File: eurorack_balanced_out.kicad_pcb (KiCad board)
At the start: 2 copper layers, 60 x 35 mm, 31 parts, among them J1 Conn_01x02, J2 Conn_01x02, J3 Conn_02x05_Odd_Even, J4 AudioJack3, J5 AudioJack3, U1 THAT1646W16, U2 THAT1646W16

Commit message: fix silkscreen
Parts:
- removed J2: Conn_01x02, Connector_PinHeader_2.54mm:PinHeader_1x02_P2.54mm_Vertical
- added Right in: Conn_01x02, Connector_PinHeader_2.54mm:PinHeader_1x02_P2.54mm_Vertical, F.Cu at (155.0, 144.5)
- Left in: renamed from J1
- Left out: renamed from J5
- Power in: renamed from J3
- Right out: renamed from J4
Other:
- board text added: "Patchnut eurorack balanced output https://github.com/mendelt/eurorack_balanced_out"
- board text added: "balanced stereo outs"
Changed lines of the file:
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@@
   (general
     (thickness 1.6)
-    (drawings 4)
+    (drawings 7)
     (tracks 155)
     (zones 0)
@@
     (tags "capacitor electrolytic")
     (attr smd)
-    (fp_text reference C1 (at 0 4) (layer F.SilkS)
+    (fp_text reference C1 (at 2 2.5) (layer F.SilkS)
       (effects (font (size 1 1) (thickness 0.15)))
     )
@@
     (tags "capacitor electrolytic")
     (attr smd)
-    (fp_text reference C2 (at 0 -4.35) (layer F.SilkS)
+    (fp_text reference C2 (at -1.5 -2.5) (layer F.SilkS)
       (effects (font (size 1 1) (thickness 0.15)))
     )
@@
     (tags "capacitor handsolder")
     (attr smd)
-    (fp_text reference C3 (at -2.975 0) (layer F.SilkS)
+    (fp_text reference C3 (at 3 0) (layer F.SilkS)
       (effects (font (size 1 1) (thickness 0.15)))
     )
@@
     (tags "capacitor electrolytic")
     (attr smd)
-    (fp_text reference C5 (at 0 -3.7 90) (layer F.SilkS)
+    (fp_text reference C5 (at -5 0 90) (layer F.SilkS)
       (effects (font (size 1 1) (thickness 0.15)))
     )
@@
     (tags "capacitor electrolytic")
     (attr smd)
-    (fp_text reference C6 (at 0 -3.7 90) (layer F.SilkS)
+    (fp_text reference C6 (at -5 0 90) (layer F.SilkS)
       (effects (font (size 1 1) (thickness 0.15)))
     )
@@
     (tags "capacitor electrolytic")
     (attr smd)
-    (fp_text reference C7 (at 0 -3.7 90) (layer F.SilkS)
+    (fp_text reference C7 (at -5 0 90) (layer F.SilkS)
       (effects (font (size 1 1) (thickness 0.15)))
     )
@@
     (tags "capacitor electrolytic")
     (attr smd)
-    (fp_text reference C8 (at 0 -3.7 90) (layer F.SilkS)
+    (fp_text reference C8 (at -5 0 90) (layer F.SilkS)
       (effects (font (size 1 1) (thickness 0.15)))
     )
@@
     (tags SOT-23)
     (attr smd)
-    (fp_text reference D1 (at -3 0) (layer F.SilkS)
+    (fp_text reference D1 (at 0.5 -2.5) (layer F.SilkS)
       (effects (font (size 1 1) (thickness 0.15)))
     )
@@
     (tags SOT-23)
     (attr smd)
-    (fp_text reference D2 (at -3 0) (layer F.SilkS)
+    (fp_text reference D2 (at 0.5 -2.5) (layer F.SilkS)
       (effects (font (size 1 1) (thickness 0.15)))
     )
@@
     (tags SOT-23)
     (attr smd)
-    (fp_text reference D3 (at -3 0) (layer F.SilkS)
+    (fp_text reference D3 (at -1 2.5) (layer F.SilkS)
       (effects (font (size 1 1) (thickness 0.15)))
     )
@@
     (tags SOT-23)
     (attr smd)
-    (fp_text reference D4 (at -3 0) (layer F.SilkS)
+    (fp_text reference D4 (at -1.5 2.5) (layer F.SilkS)
       (effects (font (size 1 1) (thickness 0.15)))
     )
@@
     (descr "Through hole straight pin header, 1x02, 2.54mm pitch, single row")
     (tags "Through hole pin header THT 1x02 2.54mm single row")
-    (fp_text reference J1 (at 0 -2.33) (layer F.SilkS)
+    (fp_text reference "Left in" (at 0 -2.96) (layer F.SilkS)
       (effects (font (size 1 1) (thickness 0.15)))
     )
@@
     (descr "Through hole straight pin header, 1x02, 2.54mm pitch, single row")
     (tags "Through hole pin header THT 1x02 2.54mm single row")
-    (fp_text reference J2 (at 0 -2.33) (layer F.SilkS)
+    (fp_text reference "Right in" (at 0 -2.96) (layer F.SilkS)
       (effects (font (size 1 1) (thickness 0.15)))
     )
@@
     (descr "6.35mm (1/4 in) Vertical Jack, Non-switching stereo jack (T/R/S), https://www.neutrik.com/en/product/nj3fd-v")
     (tags "neutrik jack vertical")
-    (fp_text reference J4 (at 0 3) (layer B.SilkS)
+    (fp_text reference "Right out" (at 0 3) (layer B.SilkS)
       (effects (font (size 1 1) (thickness 0.15)) (justify mirror))
     )
@@
     (descr "6.35mm (1/4 in) Vertical Jack, Non-switching stereo jack (T/R/S), https://www.neutrik.com/en/product/nj3fd-v")
     (tags "neutrik jack vertical")
-    (fp_text reference J5 (at 0 3) (layer B.SilkS)
+    (fp_text reference "Left out" (at 0 3) (layer B.SilkS)
       (effects (font (size 1 1) (thickness 0.15)) (justify mirror))
     )
@@
     (descr "Through hole straight pin header, 2x05, 2.54mm pitch, double rows")
     (tags "Through hole pin header THT 2x05 2.54mm double row")
-    (fp_text reference J3 (at 1.27 -2.33 90) (layer F.SilkS)
+    (fp_text reference "Power in" (at -0.46 -4.88) (layer F.SilkS)
       (effects (font (size 1 1) (thickness 0.15)))
     )
@@
       (rotate (xyz 0 0 0))
     )
+  )
+  (gr_text "Patchnut eurorack balanced output\nhttps://github.com/mendelt/eurorack_balanced_out" (at 179 136) (layer B.SilkS)
+    (effects (font (size 1 1) (thickness 0.15)) (justify left mirror))
+  )
+  (gr_line (start 121 116) (end 121 121.5) (layer F.SilkS) (width 0.3))
+  (gr_text "balanced stereo outs" (at 105 -98.6) (layer F.SilkS)
+    (effects (font (size 1 1) (thickness 0.15)))
   )
   (gr_line (start 120 115) (end 120 150) (layer Edge.Cuts) (width 0.05))
@@
   (segment (start 166 134.97) (end 163.375 137.595) (width 0.5) (layer F.Cu) (net 10))
   (segment (start 166 130.05) (end 166 134.97) (width 0.5) (layer F.Cu) (net 10))
+  (segment (start 163.375 137.595) (end 162.35 137.595) (width 0.5) (layer F.Cu) (net 10))
   (segment (start 164.5 138.72) (end 163.375 137.595) (width 0.5) (layer F.Cu) (net 10))
-  (segment (start 163.375 137.595) (end 162.35 137.595) (width 0.5) (layer F.Cu) (net 10))
   (segment (start 164.5 146) (end 164.5 138.72) (width 0.5) (layer F.Cu) (net 10))
   (segment (start 158.335 138.865) (end 158 139.2) (width 0.5) (layer F.Cu) (net 11))

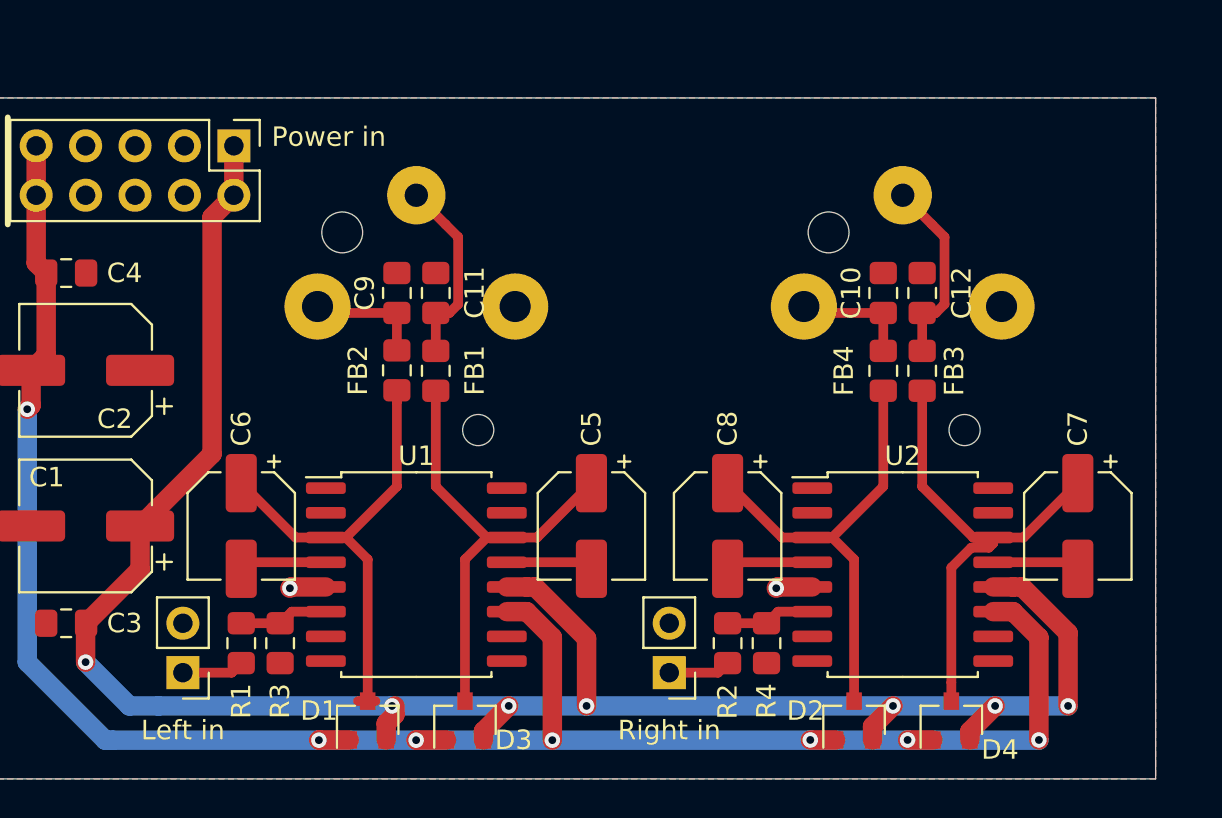
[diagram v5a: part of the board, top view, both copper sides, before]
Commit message: use different footprint for 10uF cap so we can use the 25V version
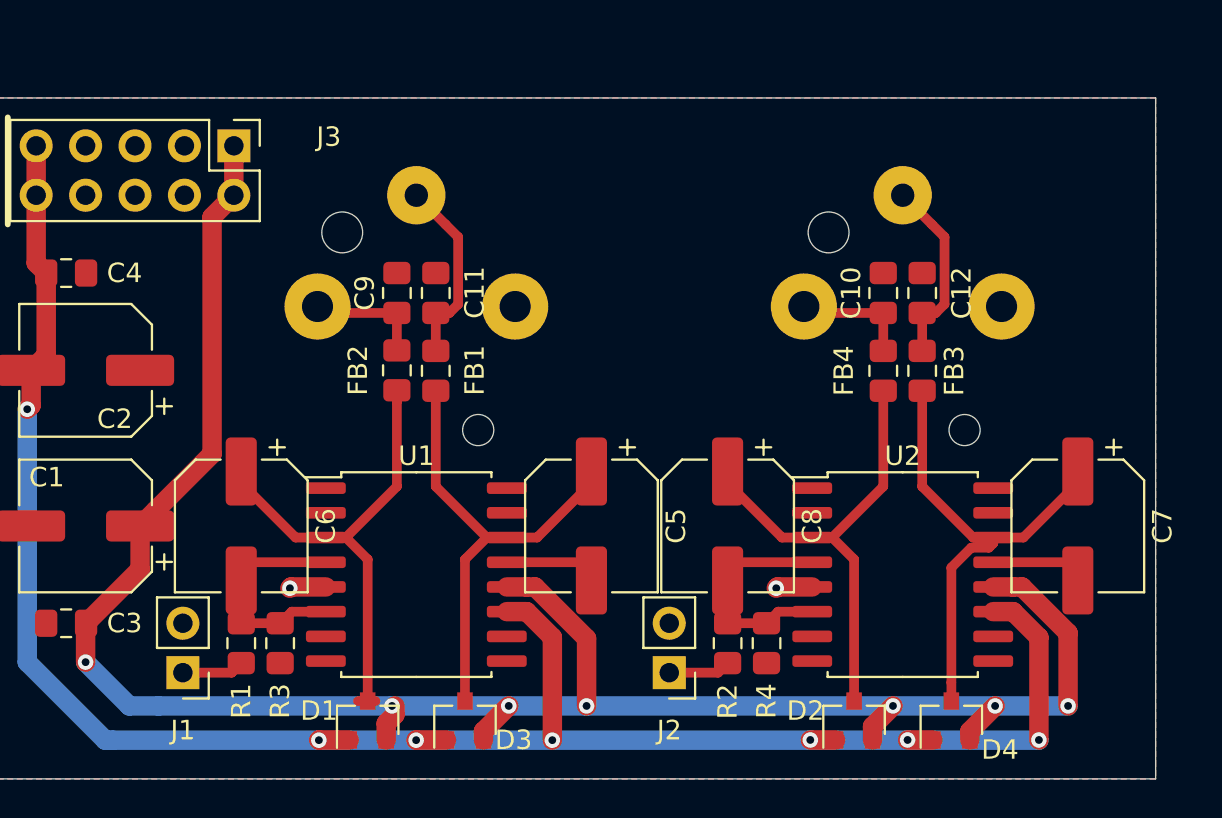
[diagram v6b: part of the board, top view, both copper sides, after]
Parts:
- C5, C6, C7, C8: footprint Capacitor_SMD:CP_Elec_5x5.4 -> Capacitor_SMD:CP_Elec_6.3x5.4
- J1: renamed from Left in
- J2: renamed from Right in
- J3: renamed from Power in
- J4: renamed from Right out
- J5: renamed from Left out
- R3, R4: value 3.9k -> 1.2k
